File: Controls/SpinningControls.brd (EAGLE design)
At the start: 209.6 x 101.6 mm, 46 parts, among them IC1 S-19246E33H-V5T2U, IC2 SN74LVC1G34DBVR, IC3 SN74LVC1G34DBVR, IC4 SN74LVC1G34DBVR, J10 SULLINS_PPPC062LFBN-RCSULLINS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, J11 SULLINS_PPPC062LFBN-RCSULLINS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, J12 SULLINS_PPPC062LFBN-RCSULLINS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, J13 SULLINS_PPPC062LFBN-RCSULLINS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, J14 SULLINS_PPPC062LFBN-RCSULLINS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, J15 430450612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

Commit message: full schematic, silkscreen cleanup
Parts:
- moved IC3 30.8 mm to (129.9, 44.7)
- moved IC4 30.4 mm to (129.9, 37.1)
- moved IC2 30.2 mm to (129.9, 40.9)
- moved FPGA 6.65 mm to (52.5, 22.4)
- moved J2 3.81 mm to (25.4, 2.54)
- moved J18 1.27 mm to (60.1, 96.4)
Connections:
- net ENC_POS: now also FPGA.41
- net ENC_POS0: now also FPGA.43
- net G1: now also FPGA.62; no longer FPGA.77
- net G2: now also FPGA.60; no longer FPGA.75
- net G3: now also FPGA.58; no longer FPGA.73
- net G4: now also FPGA.56; no longer FPGA.71
- net G5: now also FPGA.54; no longer FPGA.67
- net GSCLK_FPGA: now also FPGA.79
- net LAT_FPGA: now also FPGA.39
- net R8: now also FPGA.64; no longer FPGA.79
- net SCLK_FPGA: now also FPGA.40
- net SIN12_J10: now also FPGA.21
- net SIN12_J11: now also FPGA.17
- net SIN12_J12: now also FPGA.13
- net SIN12_J13: now also FPGA.7
- net SIN12_J14: now also FPGA.2
- net SIN12_J3: now also FPGA.50
- net SIN12_J4: now also FPGA.59
- net SIN12_J5: now also FPGA.67
- net SIN12_J6: now also FPGA.77
- net SIN12_J7: now also FPGA.35
- net SIN12_J8: now also FPGA.31
- net SIN12_J9: now also FPGA.25
- net SIN34_J10: now also FPGA.22
- net SIN34_J11: now also FPGA.18
- net SIN34_J12: now also FPGA.14
- net SIN34_J13: now also FPGA.8
- net SIN34_J14: now also FPGA.4
- net SIN34_J3: now also FPGA.49
- net SIN34_J4: now also FPGA.57
- net SIN34_J5: now also FPGA.65
- net SIN34_J6: now also FPGA.75
- net SIN34_J7: now also FPGA.36
- net SIN34_J8: now also FPGA.32
- net SIN34_J9: now also FPGA.26
- net SIN56_J10: now also FPGA.23
- net SIN56_J11: now also FPGA.19
- net SIN56_J12: now also FPGA.15
- net SIN56_J13: now also FPGA.9
- net SIN56_J14: now also FPGA.5
- net SIN56_J3: now also FPGA.47
- net SIN56_J4: now also FPGA.55
- net SIN56_J5: now also FPGA.63
- net SIN56_J6: now also FPGA.73
- net SIN56_J7: now also FPGA.37
- net SIN56_J8: now also FPGA.33
- net SIN56_J9: now also FPGA.27
- net SIN78_J10: now also FPGA.24
- net SIN78_J11: now also FPGA.20
- net SIN78_J12: now also FPGA.16
- net SIN78_J13: now also FPGA.10
- net SIN78_J14: now also FPGA.6
- net SIN78_J3: now also FPGA.45
- net SIN78_J4: now also FPGA.53
- net SIN78_J5: now also FPGA.61
- net SIN78_J6: now also FPGA.71
- net SIN78_J7: now also FPGA.38
- net SIN78_J8: now also FPGA.34
- net SIN78_J9: now also FPGA.28
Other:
- board size 209.6 x 101.6 mm -> 209.6 x 107.9 mm

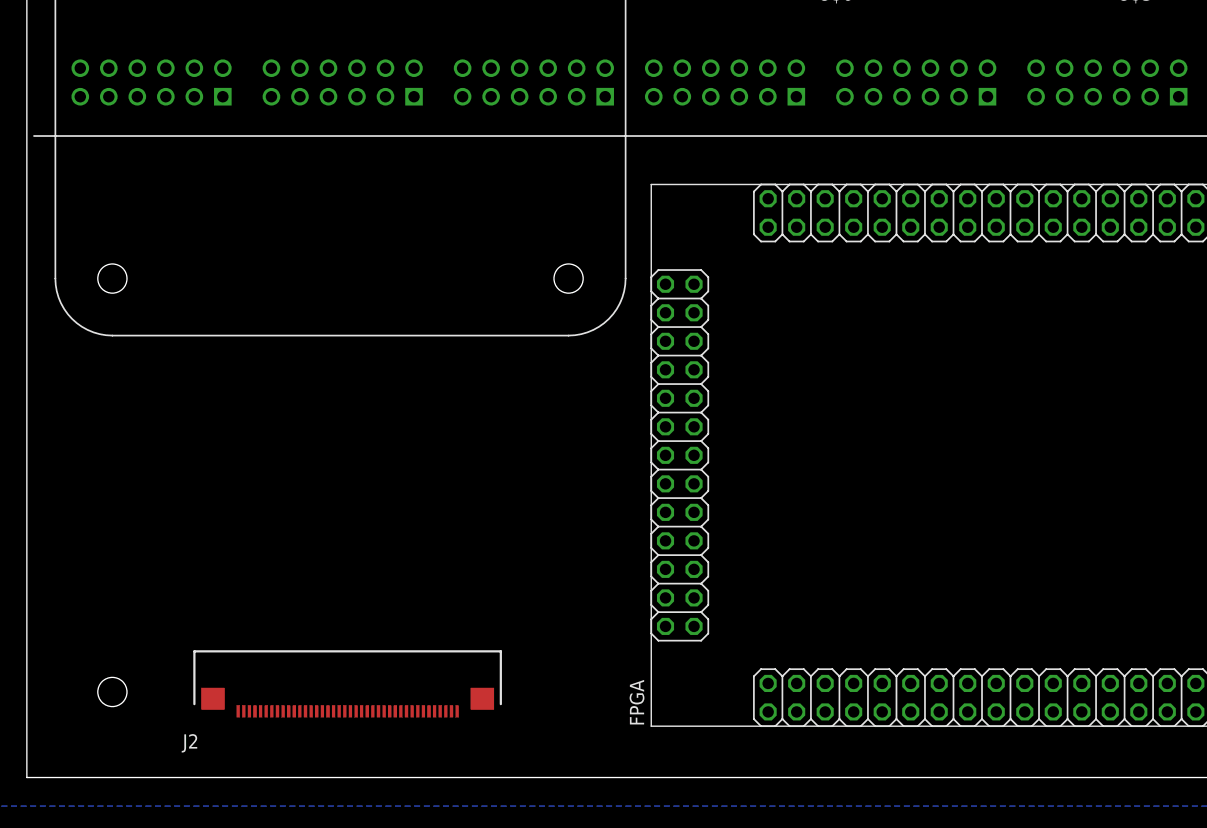
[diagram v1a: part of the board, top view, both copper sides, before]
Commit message: Started some traces
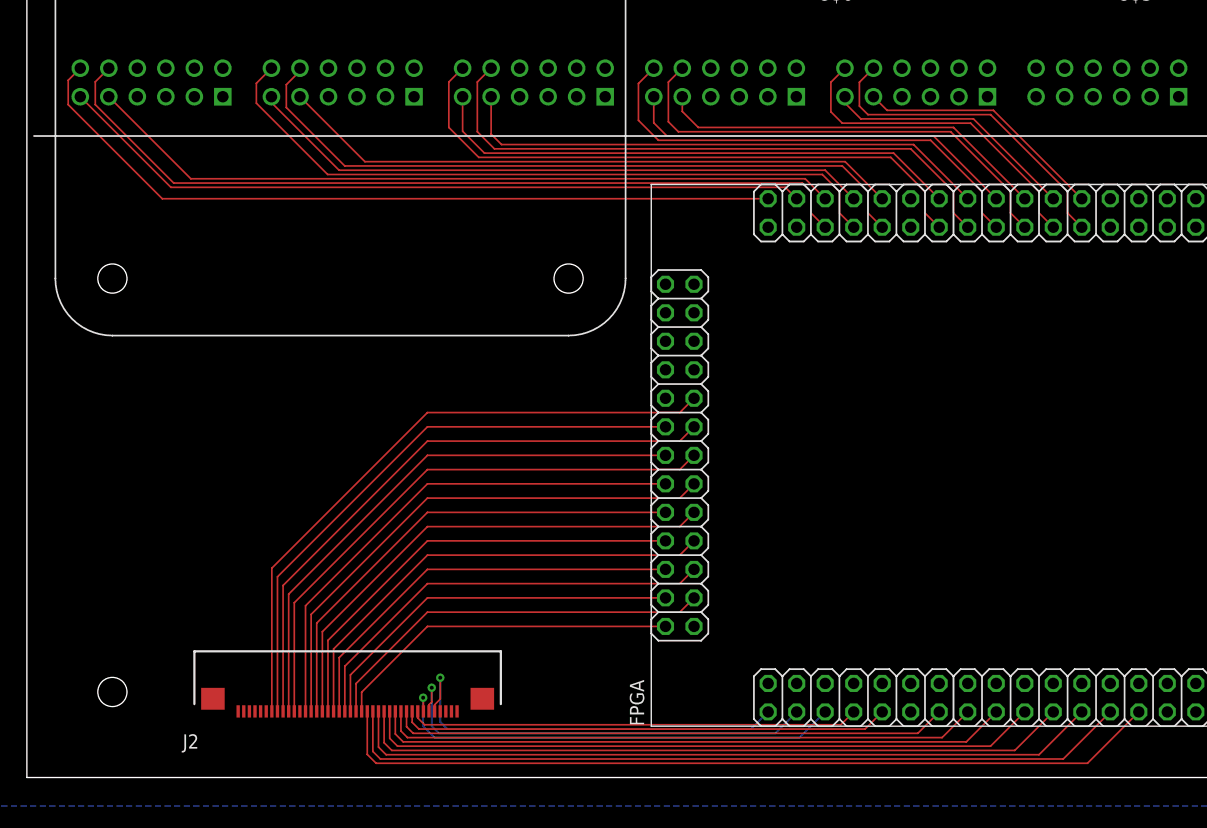
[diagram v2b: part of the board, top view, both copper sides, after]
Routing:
- net G5: track 0.00 -> 74.8 mm
- net SIN56_J14: track 0.00 -> 74.4 mm
- net G4: track 0.00 -> 71.3 mm
- net SIN12_J14: track 0.00 -> 69.5 mm
- net G3: track 0.00 -> 67.7 mm
- net SIN78_J14: track 0.00 -> 67.6 mm
- net SIN34_J14: track 0.00 -> 67.6 mm
- net G2: track 0.00 -> 64.1 mm
- net SIN56_J13: track 0.00 -> 62.6 mm
- net SIN12_J13: track 0.00 -> 62.6 mm
- net G1: track 0.00 -> 60.5 mm
- net R8: track 0.00 -> 56.9 mm
- net DISPEN: track 0.00 -> 56.6 mm
- net SIN34_J13: track 0.00 -> 55.9 mm
- net SIN78_J13: track 0.00 -> 55.6 mm
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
